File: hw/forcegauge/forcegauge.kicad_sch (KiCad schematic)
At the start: 73 parts, among them J1 USB_B_Micro, J2 Battery, J3 OLDED_Screen, J4 Load Cell, Q1 FDS6892A, Q2 BSS138, Q3 SM2331PSA P-MOSFET, Q4 S8550, Q5 FDS6892A, SW1 SW_Push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

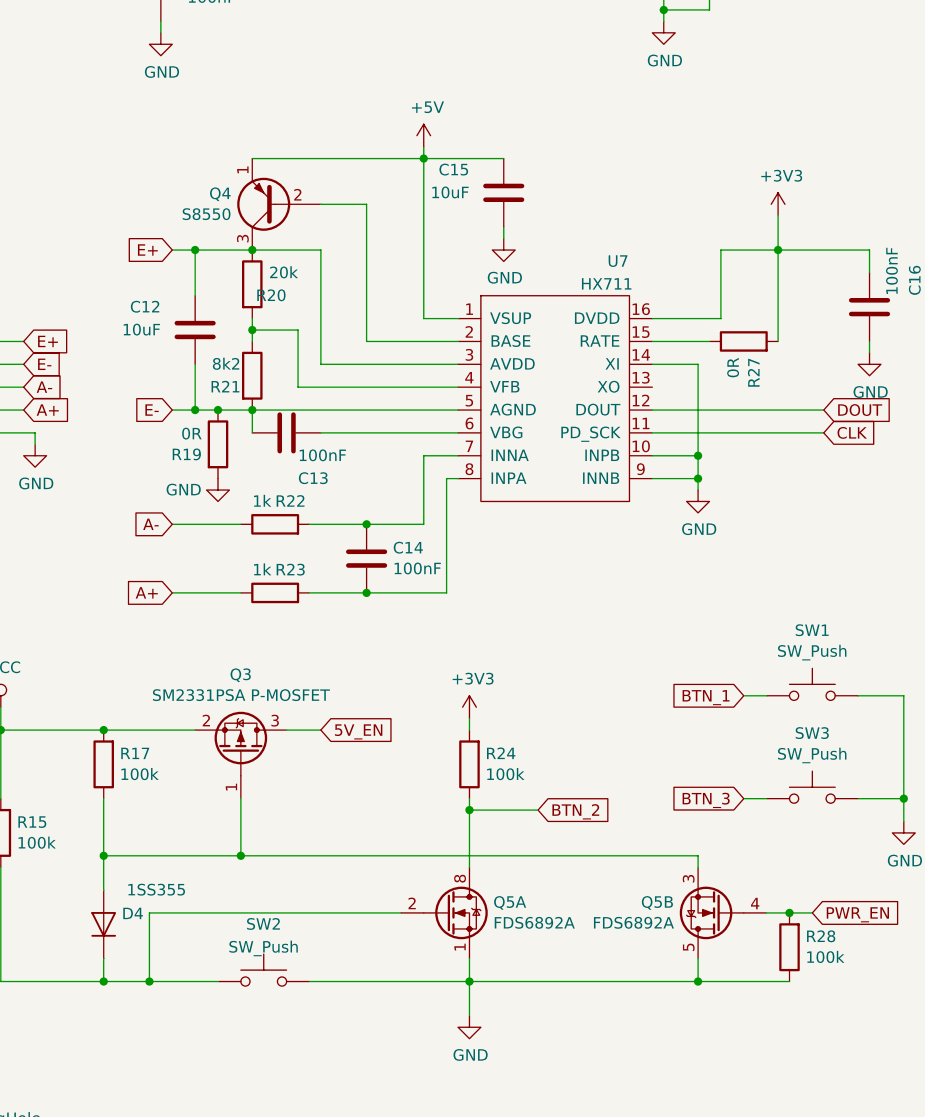
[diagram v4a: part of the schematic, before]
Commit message: button dir updated, fixed footprints and changed dual fet
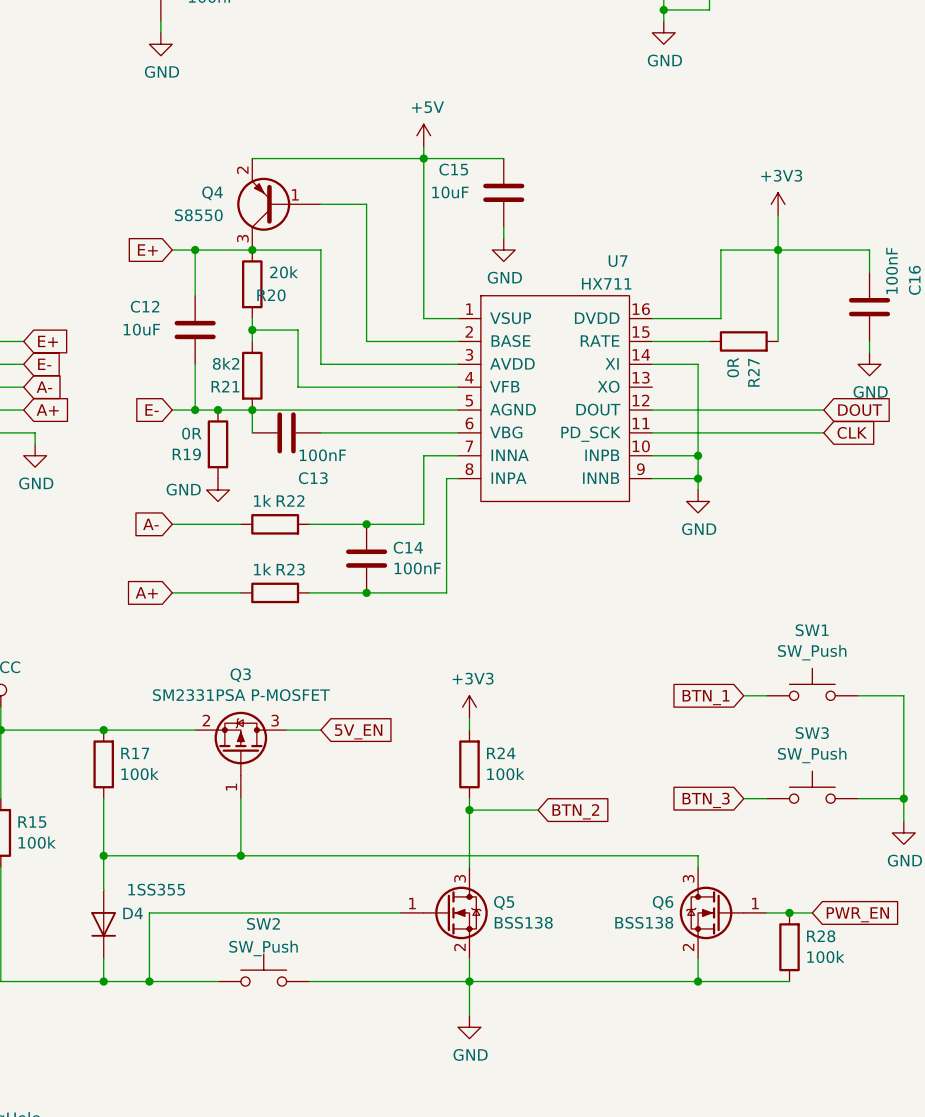
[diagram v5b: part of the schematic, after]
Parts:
- removed Q4: S8550, Package_TO_SOT_SMD:SOT-23, symbol Transistor_BJT:S8550
- removed Q5: FDS6892A, Package_SO:SOIC-8_3.9x4.9mm_P1.27mm, symbol Transistor_FET:FDS6892A
- added Q4: S8550, Package_TO_SOT_SMD:SOT-23, symbol Device:Q_PNP_BEC
- added Q5, Q6: BSS138, Package_TO_SOT_SMD:SOT-23, symbol Transistor_FET:BSS138
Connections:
- net +5V: now also Q4.2 (E)
- net BTN_2: now also Q5.3 (D)
- net E+: now also Q4.3 (C)
- net GND: now also Q5.2 (S), Q6.2 (S)
- net PWR_EN: now also Q6.1 (G)
- net at D4.1 (K), R15.1, SW2.1: now also Q5.1 (G)
- net at D4.2 (A), Q3.1 (G), R17.1: now also Q6.3 (D)
- net at U7.2 (BASE): now also Q4.1 (B)
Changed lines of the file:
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@@
   (junction (at 171.45 135.89) (diameter 0) (color 0 0 0 0)
   )
+  (junction (at 248.92 163.83) (diameter 0) (color 0 0 0 0)
+  )
   (junction (at 81.28 67.31) (diameter 0) (color 0 0 0 0)
   )
@@
   (junction (at 33.02 83.82) (diameter 0) (color 0 0 0 0)
   )
-  (junction (at 248.92 163.83) (diameter 0) (color 0 0 0 0)
-  )
   (junction (at 245.11 55.88) (diameter 0) (color 0 0 0 0)
   )
@@
   (junction (at 105.41 140.97) (diameter 0) (color 0 0 0 0)
   )
-  (junction (at 198.12 149.86) (diameter 0) (color 0 0 0 0)
-  )
   (junction (at 115.57 76.2) (diameter 0) (color 0 0 0 0)
   )
@@
   (junction (at 248.92 107.95) (diameter 0) (color 0 0 0 0)
   )
+  (junction (at 198.12 149.86) (diameter 0) (color 0 0 0 0)
+  )
   (junction (at 81.28 87.63) (diameter 0) (color 0 0 0 0)
   )
@@
     (stroke (width 0) (type default) (color 0 0 0 0))
   )
+  (wire (pts (xy 248.92 161.29) (xy 248.92 163.83))
+    (stroke (width 0) (type default) (color 0 0 0 0))
+  )
   (wire (pts (xy 27.94 124.46) (xy 29.21 124.46))
     (stroke (width 0) (type default) (color 0 0 0 0))
@@
     (stroke (width 0) (type default) (color 0 0 0 0))
   )
-  (wire (pts (xy 198.12 149.86) (xy 198.12 143.51))
+  (wire (pts (xy 198.12 143.51) (xy 198.12 149.86))
     (stroke (width 0) (type default) (color 0 0 0 0))
   )
@@
     (stroke (width 0) (type default) (color 0 0 0 0))
   )
+  (wire (pts (xy 248.92 149.86) (xy 198.12 149.86))
+    (stroke (width 0) (type default) (color 0 0 0 0))
+  )
   (wire (pts (xy 218.44 71.12) (xy 218.44 72.39))
     (stroke (width 0) (type default) (color 0 0 0 0))
@@
     (stroke (width 0) (type default) (color 0 0 0 0))
   )
-  (wire (pts (xy 248.92 163.83) (xy 259.08 163.83))
-    (stroke (width 0) (type default) (color 0 0 0 0))
-  )
   (wire (pts (xy 39.37 120.65) (xy 19.05 120.65))
     (stroke (width 0) (type default) (color 0 0 0 0))
@@
     (stroke (width 0) (type default) (color 0 0 0 0))
   )
-  (wire (pts (xy 198.12 149.86) (xy 248.92 149.86))
-    (stroke (width 0) (type default) (color 0 0 0 0))
-  )
-  (wire (pts (xy 248.92 161.29) (xy 248.92 163.83))
-    (stroke (width 0) (type default) (color 0 0 0 0))
-  )
   (wire (pts (xy 207.01 102.87) (xy 222.25 102.87))
     (stroke (width 0) (type default) (color 0 0 0 0))
@@
     (stroke (width 0) (type default) (color 0 0 0 0))
   )
+  (wire (pts (xy 248.92 163.83) (xy 259.08 163.83))
+    (stroke (width 0) (type default) (color 0 0 0 0))
+  )
   (wire (pts (xy 182.88 143.51) (xy 182.88 149.86))
     (stroke (width 0) (type default) (color 0 0 0 0))
@@
     (pin "2")
   )
-  (symbol (lib_id "Transistor_FET:FDS6892A") (at 220.98 156.21 0) (unit 1)
-    (in_bom yes) (on_board yes)
-    (property "Reference" "Q5" (id 0) (at 226.1616 155.0416 0)
-      (effects (font (size 1.27 1.27)) (justify left))
-    )
-    (property "Value" "FDS6892A" (id 1) (at 226.1616 157.353 0)
-      (effects (font (size 1.27 1.27)) (justify left))
-    )
-    (property "Footprint" "Package_SO:SOIC-8_3.9x4.9mm_P1.27mm" (id 2) (at 226.06 158.115 0)
-      (effects (font (size 1.27 1.27) italic) (justify left) hide)
-    )
-    (property "Datasheet" "https://www.onsemi.com/pdf/datasheet/fds6892a-d.pdf" (id 3) (at 220.98 156.21 0)
-      (effects (font (size 1.27 1.27)) (justify left) hide)
-    )
-    (pin "1")
-    (pin "2")
-    (pin "7")
-    (pin "8")
-  )
-  (symbol (lib_id "Transistor_FET:FDS6892A") (at 251.46 156.21 180) (unit 2)
-    (in_bom yes) (on_board yes)
-    (property "Reference" "Q5" (id 0) (at 246.253 155.0416 0)
-      (effects (font (size 1.27 1.27)) (justify left))
-    )
-    (property "Value" "FDS6892A" (id 1) (at 246.253 157.353 0)
-      (effects (font (size 1.27 1.27)) (justify left))
-    )
-    (property "Footprint" "Package_SO:SOIC-8_3.9x4.9mm_P1.27mm" (id 2) (at 246.38 154.305 0)
-      (effects (font (size 1.27 1.27) italic) (justify left) hide)
-    )
-    (property "Datasheet" "https://www.onsemi.com/pdf/datasheet/fds6892a-d.pdf" (id 3) (at 251.46 156.21 0)
-      (effects (font (size 1.27 1.27)) (justify left) hide)
-    )
-    (pin "3")
-    (pin "4")
-    (pin "5")
-    (pin "6")
-  )
   (symbol (lib_id "power:GND") (at 223.52 167.64 0) (unit 1)
     (in_bom yes) (on_board yes)
@@
     (pin "1")
   )
-  (symbol (lib_id "Transistor_BJT:S8550") (at 201.93 77.47 180) (unit 1)
-    (in_bom yes) (on_board yes)
-    (property "Reference" "Q4" (id 0) (at 197.0786 76.3016 0)
-      (effects (font (size 1.27 1.27)) (justify left))
-    )
-    (property "Value" "S8550" (id 1) (at 197.0786 78.613 0)
-      (effects (font (size 1.27 1.27)) (justify left))
-    )
-    (property "Footprint" "Package_TO_SOT_SMD:SOT-23" (id 2) (at 196.85 75.565 0)
-      (effects (font (size 1.27 1.27) italic) (justify left) hide)
-    )
-    (property "Datasheet" "http://www.unisonic.com.tw/datasheet/S8550.pdf" (id 3) (at 201.93 77.47 0)
-      (effects (font (size 1.27 1.27)) (justify left) hide)
-    )
-    (pin "1")
-    (pin "2")
-    (pin "3")
-  )
   (symbol (lib_id "ForceGaugeSymbols:MT3608") (at 54.61 83.82 0) (unit 1)
     (in_bom yes) (on_board yes)
@@
     (pin "2")
   )
+  (symbol (lib_id "Transistor_FET:BSS138") (at 251.46 156.21 0) (mirror y) (unit 1)
+    (in_bom yes) (on_board yes)
+    (property "Reference" "Q6" (id 0) (at 246.2784 155.0416 0)
+      (effects (font (size 1.27 1.27)) (justify left))
+    )
+    (property "Value" "BSS138" (id 1) (at 246.2784 157.353 0)
+      (effects (font (size 1.27 1.27)) (justify left))
+    )
+    (property "Footprint" "Package_TO_SOT_SMD:SOT-23" (id 2) (at 246.38 158.115 0)
+      (effects (font (size 1.27 1.27) italic) (justify left) hide)
+    )
+    (property "Datasheet" "https://www.fairchildsemi.com/datasheets/BS/BSS138.pdf" (id 3) (at 251.46 156.21 0)
+      (effects (font (size 1.27 1.27)) (justify left) hide)
+    )
+    (pin "1")
+    (pin "2")
+    (pin "3")
+  )
   (symbol (lib_id "Mechanical:MountingHole") (at 161.29 187.96 0) (unit 1)
     (in_bom yes) (on_board yes) (fields_autoplaced)
@@
     (pin "2")
   )
+  (symbol (lib_id "Device:Q_PNP_BEC") (at 201.93 77.47 180) (unit 1)
+    (in_bom yes) (on_board yes) (fields_autoplaced)
+    (property "Reference" "Q4" (id 0) (at 196.215 76.1999 0)
+      (effects (font (size 1.27 1.27)) (justify left))
+    )
+    (property "Value" "S8550" (id 1) (at 196.215 78.7399 0)
+      (effects (font (size 1.27 1.27)) (justify left))
+    )
+    (property "Footprint" "Package_TO_SOT_SMD:SOT-23" (id 2) (at 196.85 80.01 0)
+      (effects (font (size 1.27 1.27)) hide)
+    )
+    (property "Datasheet" "https://www.rcscomponents.kiev.ua/datasheets/s8550-2ty-datasheet.pdf" (id 3) (at 201.93 77.47 0)
+      (effects (font (size 1.27 1.27)) hide)
+    )
+    (pin "1")
+    (pin "2")
+    (pin "3")
+  )
   (symbol (lib_id "Mechanical:MountingHole") (at 161.29 177.8 0) (unit 1)
     (in_bom yes) (on_board yes) (fields_autoplaced)
@@
     )
   )
+  (symbol (lib_id "Transistor_FET:BSS138") (at 220.98 156.21 0) (unit 1)
+    (in_bom yes) (on_board yes)
+    (property "Reference" "Q5" (id 0) (at 226.1616 155.0416 0)
+      (effects (font (size 1.27 1.27)) (justify left))
+    )
+    (property "Value" "BSS138" (id 1) (at 226.1616 157.353 0)
+      (effects (font (size 1.27 1.27)) (justify left))
+    )
+    (property "Footprint" "Package_TO_SOT_SMD:SOT-23" (id 2) (at 226.06 158.115 0)
+      (effects (font (size 1.27 1.27) italic) (justify left) hide)
+    )
+    (property "Datasheet" "https://www.fairchildsemi.com/datasheets/BS/BSS138.pdf" (id 3) (at 220.98 156.21 0)
+      (effects (font (size 1.27 1.27)) (justify left) hide)
+    )
+    (pin "1")
+    (pin "2")
+    (pin "3")
+  )
   (sheet_instances
     (path "/" (page "1"))
@@
       (reference "Q3") (unit 1) (value "SM2331PSA P-MOSFET") (footprint "Package_TO_SOT_SMD:SOT-23")
     )
-    (path "/00000000-0000-0000-0000-000060d9e268"
+    (path "/70443cc0-9149-4285-9547-389cc032e7dc"
       (reference "Q4") (unit 1) (value "S8550") (footprint "Package_TO_SOT_SMD:SOT-23")
     )
-    (path "/00000000-0000-0000-0000-000060c1583f"
-      (reference "Q5") (unit 1) (value "FDS6892A") (footprint "Package_SO:SOIC-8_3.9x4.9mm_P1.27mm")
+    (path "/e4c5dd94-787d-4d5d-b548-d108955d9aa3"
+      (reference "Q5") (unit 1) (value "BSS138") (footprint "Package_TO_SOT_SMD:SOT-23")
     )
-    (path "/00000000-0000-0000-0000-000060c16514"
-      (reference "Q5") (unit 2) (value "FDS6892A") (footprint "Package_SO:SOIC-8_3.9x4.9mm_P1.27mm")
+    (path "/04aeee45-25fb-4b68-8389-3b1682a894f2"
+      (reference "Q6") (unit 1) (value "BSS138") (footprint "Package_TO_SOT_SMD:SOT-23")
     )
     (path "/00000000-0000-0000-0000-000060c544e2"

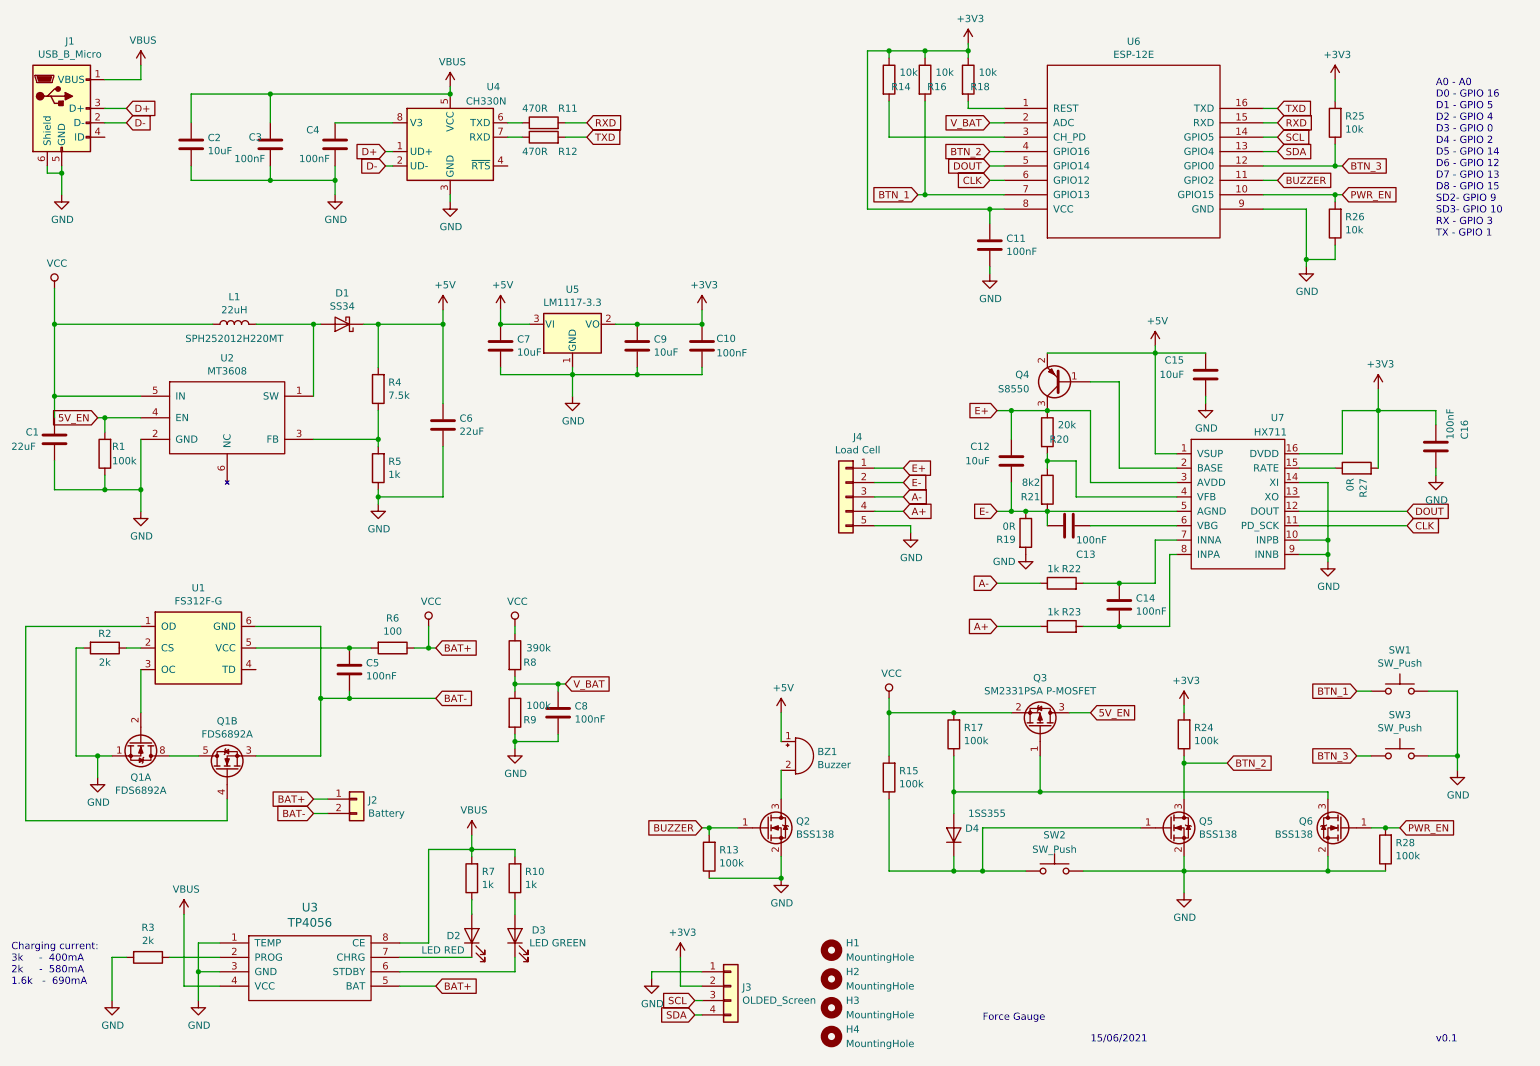
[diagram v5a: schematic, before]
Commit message: pcb v0.2 fixed errors
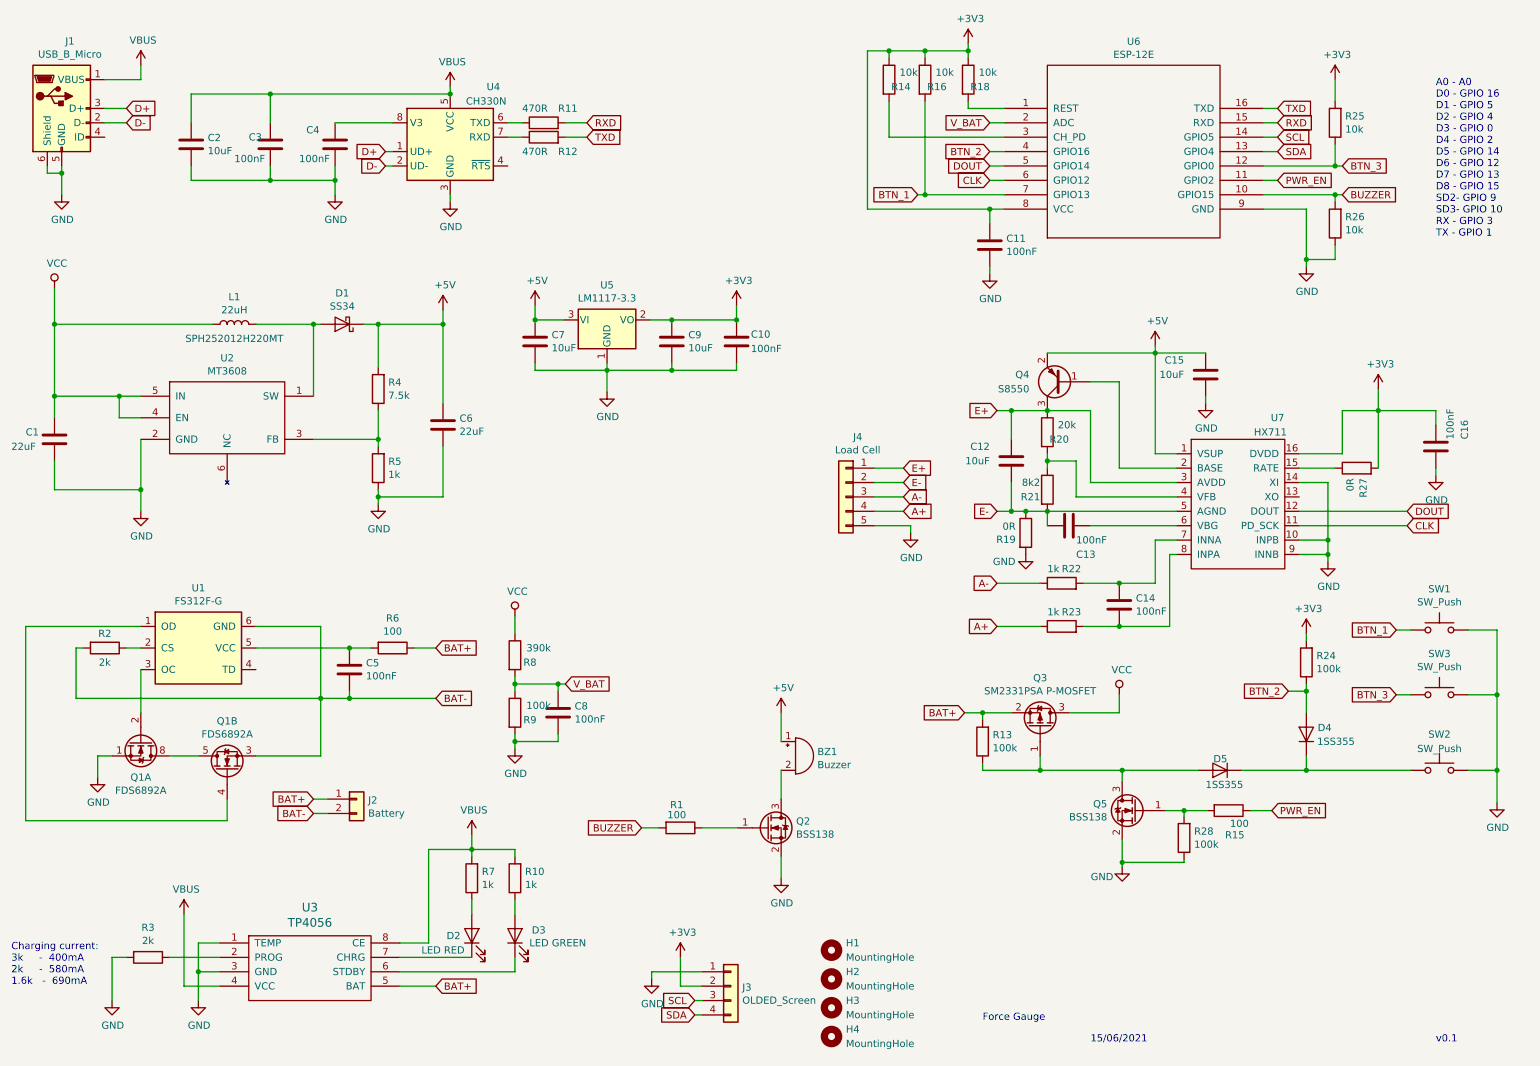
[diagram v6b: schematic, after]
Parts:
- removed Q5: BSS138, Package_TO_SOT_SMD:SOT-23, symbol Transistor_FET:BSS138
- removed R17: 100k, Resistor_SMD:R_0603_1608Metric, symbol Device:R
- added D5: 1SS355, Diode_SMD:D_SOD-323_HandSoldering, symbol Device:D
- L1: footprint Inductor_SMD:L_1008_2520Metric -> Inductor_SMD:L_Wuerth_MAPI-3012
- Q1: Alt1 (none) -> DMN2041LSD-13; Alt2 (none) -> FDS9926A
- R1, R15: value 100k -> 100
- renumbered Q6 to Q5
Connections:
- net BAT-: now also R2.2
- net BTN_2: now also D4.2 (A)
- net BUZZER: now also R1.2, R26.2, U6.10 (GPIO15); no longer Q2.1 (G), R13.2, U6.11 (GPIO2)
- net GND: no longer R1.1, R13.1, R2.2
- net PWR_EN: now also R15.1, U6.11 (GPIO2); no longer Q5.1 (G), R26.2, R28.2, U6.10 (GPIO15)
- net VCC: now also Q3.3 (D), U2.4 (EN); no longer J2.1 (Pin_1), Q3.2 (S), R15.2, R6.1, U3.5 (BAT)
- net at D4.1 (K), SW2.1: now also D5.1 (K); no longer R15.1
- net at Q3.1 (G), Q5.3 (D): now also R13.1, D5.2 (A); no longer D4.2 (A)
- removed net 5V_EN: Q3.3 (D), R1.2, U2.4 (EN)
- new net: Q5.1 (G), R15.2, R28.2
- new net: Q2.1 (G), R1.1
- new net BAT+: J2.1 (Pin_1), Q3.2 (S), R13.2, R6.1, U3.5 (BAT)
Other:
- moved on the sheet: C10, C7, C9, D4, Q5, R24, R28, SW1, SW2, SW3, U5
